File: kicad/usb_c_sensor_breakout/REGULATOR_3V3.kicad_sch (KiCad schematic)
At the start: 4 parts, among them U1 AP2112K-3.3

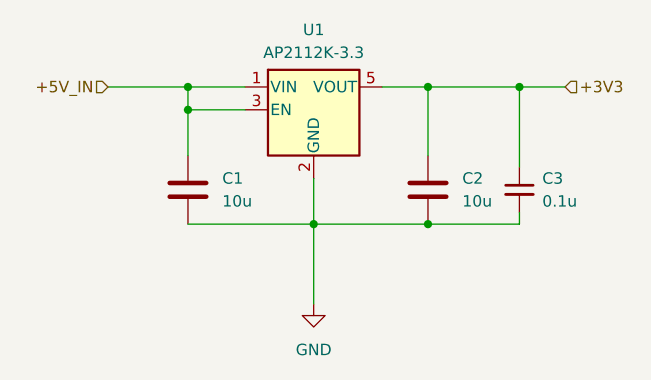
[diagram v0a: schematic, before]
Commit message: Commit3: Regulators + Top-level + I2C sensor upgrade
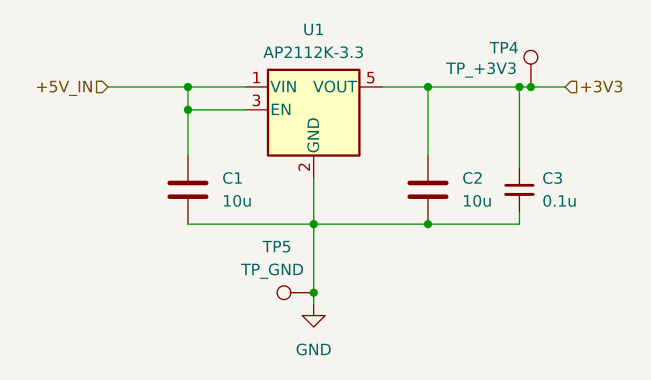
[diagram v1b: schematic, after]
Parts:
- added TP4: TP_+3V3, symbol Connector:TestPoint
- added TP5: TP_GND, symbol Connector:TestPoint
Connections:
- net +3V3: now also TP4.1
- net GND: now also TP5.1
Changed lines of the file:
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@@
+	)
+	(junction
+		(at 113.03 76.2)
+		(diameter 0)
+		(color 0 0 0 0)
+	)
+	(junction
+		(at 88.9 99.06)
+		(diameter 0)
+		(color 0 0 0 0)
 	)
 	(junction
@@
 	(wire
 		(pts
-			(xy 111.76 76.2) (xy 116.84 76.2)
+			(xy 111.76 76.2) (xy 113.03 76.2)
 		)
 		(stroke
@@
 	(wire
 		(pts
-			(xy 88.9 91.44) (xy 88.9 100.33)
+			(xy 88.9 91.44) (xy 88.9 99.06)
+		)
+		(stroke
+			(width 0)
+			(type default)
+		)
+	)
+	(wire
+		(pts
+			(xy 113.03 76.2) (xy 116.84 76.2)
+		)
+		(stroke
+			(width 0)
+			(type default)
+		)
+	)
+	(wire
+		(pts
+			(xy 88.9 99.06) (xy 88.9 100.33)
 		)
 		(stroke
@@
 	)
 	(symbol
+		(lib_id "Connector:TestPoint")
+		(at 113.03 76.2 0)
+		(unit 1)
+		(exclude_from_sim no)
+		(in_bom yes)
+		(on_board yes)
+		(dnp no)
+		(property "Reference" "TP4"
+			(at 108.458 71.882 0)
+			(effects
+				(font
+					(size 1.27 1.27)
+				)
+				(justify left)
+			)
+		)
+		(property "Value" "TP_+3V3"
+			(at 103.632 74.168 0)
+			(effects
+				(font
+					(size 1.27 1.27)
+				)
+				(justify left)
+			)
+		)
+		(property "Footprint" ""
+			(at 118.11 76.2 0)
+			(effects
+				(font
+					(size 1.27 1.27)
+				)
+				(hide yes)
+			)
+		)
+		(property "Datasheet" "~"
+			(at 118.11 76.2 0)
+			(effects
+				(font
+					(size 1.27 1.27)
+				)
+				(hide yes)
+			)
+		)
+		(property "Description" "test point"
+			(at 113.03 76.2 0)
+			(effects
+				(font
+					(size 1.27 1.27)
+				)
+				(hide yes)
+			)
+		)
+		(pin "1"
+		)
+		(instances
+			(project ""
+				(path "/a2072585-dfc7-469c-b616-14a83342abb9/447a3edd-df06-4977-9e2f-278020fd9b85"
+					(reference "TP4")
+					(unit 1)
+				)
+			)
+		)
+	)
+	(symbol
 		(lib_id "power:GND")
 		(at 88.9 100.33 0)
@@
 					(unit 1)
 				)
+			)
+		)
+	)
+	(symbol
+		(lib_id "Connector:TestPoint")
+		(at 88.9 99.06 90)
+		(unit 1)
+		(exclude_from_sim no)
+		(in_bom yes)
+		(on_board yes)
+		(dnp no)
+		(property "Reference" "TP5"
+			(at 84.836 93.98 90)
+			(effects
+				(font
+					(size 1.27 1.27)
+				)
+			)
+		)
+		(property "Value" "TP_GND"
+			(at 84.328 96.52 90)
+			(effects
+				(font
+					(size 1.27 1.27)
+				)
+			)
+		)
+		(property "Footprint" ""
+			(at 88.9 93.98 0)
+			(effects
+				(font
+					(size 1.27 1.27)
+				)
+				(hide yes)
+			)
+		)
+		(property "Datasheet" "~"
+			(at 88.9 93.98 0)
+			(effects
+				(font
+					(size 1.27 1.27)
+				)
+				(hide yes)
+			)
+		)
+		(property "Description" "test point"
+			(at 88.9 99.06 0)
+			(effects
+				(font
+					(size 1.27 1.27)
+				)
+				(hide yes)
+			)
+		)
+		(pin "1"
+		)
+		(instances
+			(project ""
+				(path "/a2072585-dfc7-469c-b616-14a83342abb9/447a3edd-df06-4977-9e2f-278020fd9b85"
+					(reference "TP5")
+					(unit 1)
+				)

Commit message: Commit 4: Updated annotation + footprints
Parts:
- C1, C2, C3: footprint (none) -> Capacitor_SMD:C_0603_1608Metric
- TP4, TP5: footprint (none) -> TestPoint:TestPoint_Pad_D1.5mm
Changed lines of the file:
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@@
 			)
 		)
-		(property "Footprint" ""
+		(property "Footprint" "Capacitor_SMD:C_0603_1608Metric"
 			(at 111.76 87.63 0)
 			(effects
@@
 			)
 		)
-		(property "Footprint" ""
+		(property "Footprint" "Capacitor_SMD:C_0603_1608Metric"
 			(at 73.9648 83.82 0)
 			(effects
@@
 			)
 		)
-		(property "Footprint" ""
+		(property "Footprint" "Capacitor_SMD:C_0603_1608Metric"
 			(at 100.6348 83.82 0)
 			(effects
@@
 			)
 		)
-		(property "Footprint" ""
+		(property "Footprint" "TestPoint:TestPoint_Pad_D1.5mm"
 			(at 118.11 76.2 0)
 			(effects
@@
 			)
 		)
-		(property "Footprint" ""
+		(property "Footprint" "TestPoint:TestPoint_Pad_D1.5mm"
 			(at 88.9 93.98 0)
 			(effects

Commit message: Commit 6: Finished PCB + Updated Schematic
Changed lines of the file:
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@@
 	)
 	(hierarchical_label "+3V3"
-		(shape input)
+		(shape output)
 		(at 116.84 76.2 0)
 		(effects
